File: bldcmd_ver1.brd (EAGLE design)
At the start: 43 x 49 mm, 84 parts, among them CN1 DF61-2P-2.2V(23), CN2 DF65-3P-1.7V(21), CN3 DF57H-5P-1.2V(21), CN5 SM04B-SRSS-TB, CN6 SM05B-SRSS-TB, CN7 SM04B-SRSS-TB, IC1 STSPIN32F0A, IC2 AS5047P-ATSM, IC4 LTC485S, Q1 PSMN2R4-30MLD, Q2 PSMN2R4-30MLD, Q3 PSMN2R4-30MLD, Q4 PSMN2R4-30MLD, Q5 PSMN2R4-30MLD, Q6 PSMN2R4-30MLD, SW1 SKRP

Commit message: AW進捗
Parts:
- moved R6 2.71 mm to (6.00, 16.2)
- moved R3 0.70 mm to (7.00, 33.0)
- moved R27 0.20 mm to (20.1, 1.50)
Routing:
- net GND: track 283.1 -> 298.8 mm
- net MOT_U: track 43.8 -> 47.3 mm, vias 11 -> 14
- net N$16: track 1.35 -> 4.26 mm
- net LS_W: track 15.1 -> 12.3 mm
- net MOT_W: track 39.1 -> 38.3 mm
- net OC_COMP: track 4.51 -> 3.66 mm
- net N$13: track 3.35 -> 2.65 mm
- net LS_U: track 34.1 -> 33.4 mm

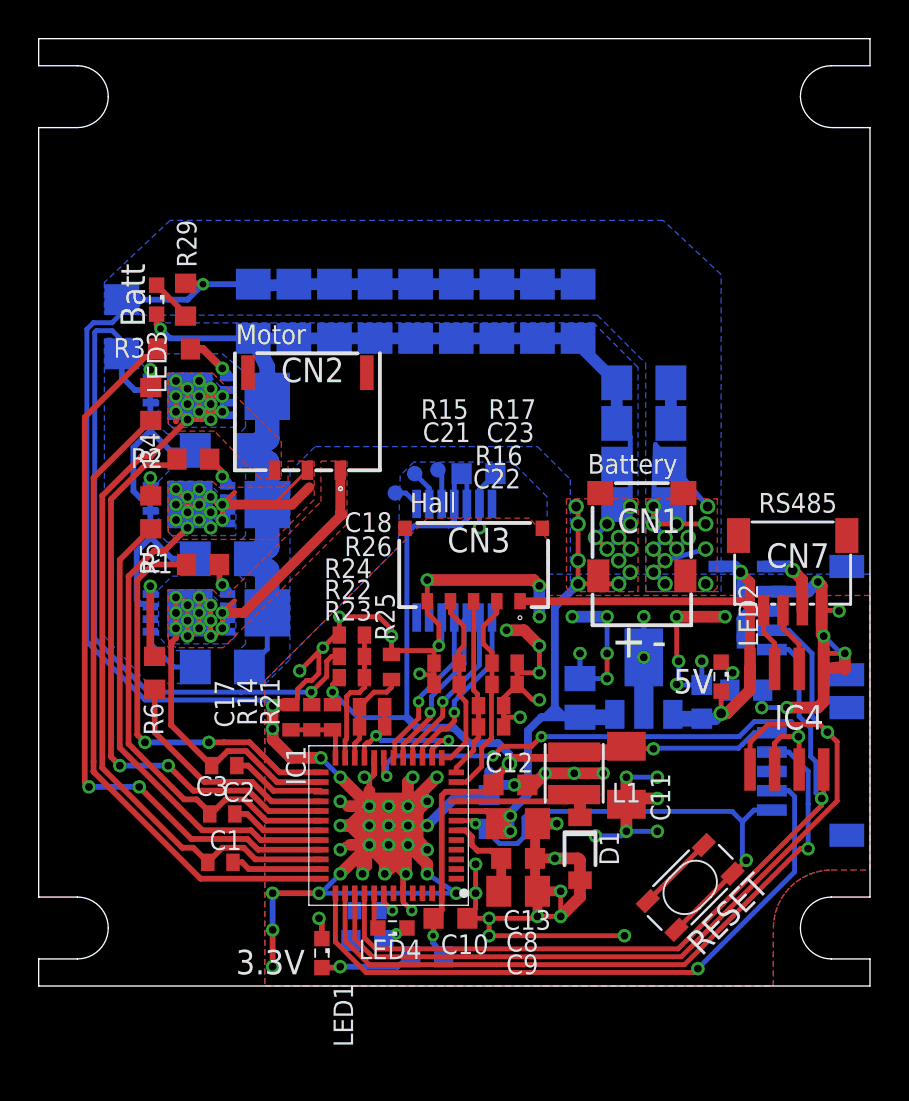
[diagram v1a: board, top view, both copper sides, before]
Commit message: 基板サイズを変更した
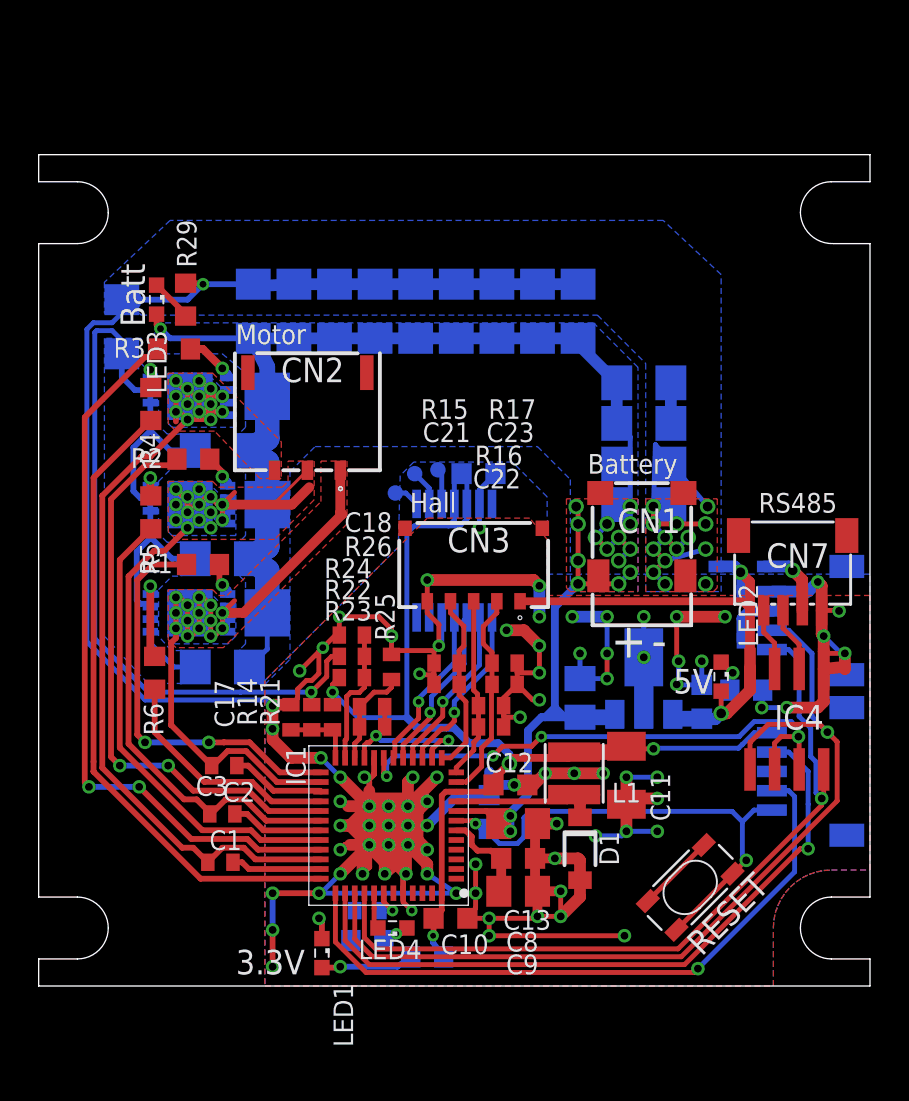
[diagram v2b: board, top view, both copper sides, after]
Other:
- board size 43 x 49 mm -> 43 x 43 mm
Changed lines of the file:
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@@
 <setting verticaltext="up"/>
 </settings>
-<grid distance="0.1" unitdist="mm" unit="mm" style="lines" multiple="1" display="yes" altdistance="0.05" altunitdist="mm" altunit="mm"/>
+<grid distance="1" unitdist="mm" unit="mm" style="lines" multiple="1" display="yes" altdistance="0.05" altunitdist="mm" altunit="mm"/>
 <layers>
-<layer number="1" name="Top" color="4" fill="1" visible="yes" active="yes"/>
+<layer number="1" name="Top" color="4" fill="1" visible="no" active="yes"/>
 <layer number="2" name="Route2" color="1" fill="3" visible="no" active="no"/>
 <layer number="3" name="Route3" color="4" fill="3" visible="no" active="no"/>
@@
 <layer number="19" name="Unrouted" color="6" fill="1" visible="yes" active="yes"/>
 <layer number="20" name="Dimension" color="24" fill="1" visible="yes" active="yes"/>
-<layer number="21" name="tPlace" color="31" fill="1" visible="yes" active="yes"/>
+<layer number="21" name="tPlace" color="31" fill="1" visible="no" active="yes"/>
 <layer number="22" name="bPlace" color="25" fill="10" visible="yes" active="yes"/>
-<layer number="23" name="tOrigins" color="15" fill="1" visible="yes" active="yes"/>
+<layer number="23" name="tOrigins" color="15" fill="1" visible="no" active="yes"/>
 <layer number="24" name="bOrigins" color="15" fill="1" visible="yes" active="yes"/>
 <layer number="25" name="tNames" color="11" fill="7" visible="no" active="yes"/>
-<layer number="26" name="bNames" color="13" fill="7" visible="no" active="yes"/>
+<layer number="26" name="bNames" color="13" fill="7" visible="yes" active="yes"/>
 <layer number="27" name="tValues" color="7" fill="1" visible="no" active="yes"/>
 <layer number="28" name="bValues" color="7" fill="1" visible="no" active="yes"/>
-<layer number="29" name="tStop" color="7" fill="3" visible="yes" active="yes"/>
+<layer number="29" name="tStop" color="7" fill="3" visible="no" active="yes"/>
 <layer number="30" name="bStop" color="7" fill="6" visible="yes" active="yes"/>
 <layer number="31" name="tCream" color="7" fill="4" visible="no" active="yes"/>
@@
 <layer number="37" name="tTest" color="7" fill="1" visible="no" active="yes"/>
 <layer number="38" name="bTest" color="7" fill="1" visible="no" active="yes"/>
-<layer number="39" name="tKeepout" color="4" fill="11" visible="yes" active="yes"/>
+<layer number="39" name="tKeepout" color="4" fill="11" visible="no" active="yes"/>
 <layer number="40" name="bKeepout" color="1" fill="11" visible="yes" active="yes"/>
 <layer number="41" name="tRestrict" color="4" fill="10" visible="no" active="yes"/>
@@
 <layer number="47" name="Measures" color="7" fill="1" visible="yes" active="yes"/>
 <layer number="48" name="Document" color="7" fill="1" visible="yes" active="yes"/>
-<layer number="49" name="Reference" color="18" fill="1" visible="yes" active="yes"/>
+<layer number="49" name="Reference" color="18" fill="1" visible="no" active="yes"/>
 <layer number="50" name="dxf" color="7" fill="1" visible="yes" active="yes"/>
-<layer number="51" name="tDocu" color="14" fill="1" visible="yes" active="yes"/>
+<layer number="51" name="tDocu" color="14" fill="1" visible="no" active="yes"/>
 <layer number="52" name="bDocu" color="11" fill="1" visible="yes" active="yes"/>
 <layer number="53" name="tGND_GNDA" color="7" fill="1" visible="yes" active="yes"/>
@@
 </layers>
 <board>
-<fusionsync huburn="a.cGVyc29uYWw6dWUyOTdmOTdk" projecturn="a.cGVyc29uYWw6dWUyOTdmOTdkIzIwMTYwMTIwMjMzNzY0MzE" f3durn="urn:adsk.wipprod:dm.lineage:Rlxp0FusTXWNQhIXcPZ1tQ" pcbguid="3740698e-3e28-4753-a590-d83306e07c12" lastpulledtime="" lastsyncedchangeguid="09eb6062-57fd-4b9e-7a9e-39c488cf4b4b"/>
+<fusionsync huburn="a.cGVyc29uYWw6dWUyOTdmOTdk" projecturn="a.cGVyc29uYWw6dWUyOTdmOTdkIzIwMTYwMTIwMjMzNzY0MzE" f3durn="urn:adsk.wipprod:dm.lineage:Rlxp0FusTXWNQhIXcPZ1tQ" pcbguid="3740698e-3e28-4753-a590-d83306e07c12" lastpulledtime="" lastsyncedchangeguid="25f6fb32-d5f4-c03e-7a0e-6774be7ba0ba"/>
 <plain>
 <wire x1="0" y1="0" x2="43" y2="0" width="0" layer="20"/>
@@
 BLDC_MotorDriver
 v1.1</text>
-<dimension x1="0" y1="0" x2="43" y2="0" x3="21.5" y3="-19.4" textsize="1.778" layer="48"/>
-<dimension x1="0" y1="0" x2="0" y2="49" x3="-10.8" y3="24.5" textsize="1.778" layer="48"/>
-<dimension x1="0" y1="49" x2="43" y2="49" x3="21.5" y3="60.8" textsize="1.778" layer="48"/>
-<dimension x1="43" y1="49" x2="43" y2="0" x3="63.8" y3="24.5" textsize="1.778" layer="48"/>
+<dimension x1="0" y1="-1" x2="43" y2="-1" x3="21.5" y3="-8.4" textsize="1.778" layer="48"/>
+<dimension x1="-1" y1="0" x2="-1" y2="43" x3="-6.8" y3="21.5" textsize="1.778" layer="48"/>
+<dimension x1="0" y1="44" x2="43" y2="44" x3="21.5" y3="48.8" textsize="1.778" layer="48"/>
+<dimension x1="44" y1="43" x2="44" y2="0" x3="50.800003125" y3="21.5" textsize="1.778" layer="48"/>
 <wire x1="43" y1="0" x2="43" y2="1.4" width="0" layer="20"/>
 <wire x1="43" y1="1.4" x2="41" y2="1.4" width="0" layer="20"/>
@@
 <wire x1="39.4" y1="3" x2="41" y2="4.6" width="0" layer="20" curve="-90"/>
 <wire x1="41" y1="4.6" x2="43" y2="4.6" width="0" layer="20"/>
-<wire x1="43" y1="4.6" x2="43" y2="44.4" width="0" layer="20"/>
-<wire x1="43" y1="44.4" x2="41.1" y2="44.4" width="0" layer="20"/>
-<wire x1="41.1" y1="44.4" x2="39.4" y2="46" width="0" layer="20" curve="-90"/>
-<wire x1="39.4" y1="46" x2="41" y2="47.6" width="0" layer="20" curve="-90"/>
-<wire x1="41" y1="47.6" x2="43" y2="47.6" width="0" layer="20"/>
-<wire x1="43" y1="47.6" x2="43" y2="49" width="0" layer="20"/>
-<wire x1="43" y1="49" x2="0" y2="49" width="0" layer="20"/>
-<wire x1="0" y1="49" x2="0" y2="47.6" width="0" layer="20"/>
-<wire x1="0" y1="47.6" x2="2" y2="47.6" width="0" layer="20"/>
-<wire x1="2" y1="47.6" x2="3.6" y2="46" width="0" layer="20" curve="-90"/>
-<wire x1="3.6" y1="46" x2="2" y2="44.4" width="0" layer="20" curve="-90"/>
-<wire x1="2" y1="44.4" x2="0" y2="44.4" width="0" layer="20"/>
-<wire x1="0" y1="44.4" x2="0" y2="4.6" width="0" layer="20"/>
+<wire x1="43" y1="4.6" x2="43" y2="38.4" width="0" layer="20"/>
+<wire x1="43" y1="38.4" x2="41.1" y2="38.4" width="0" layer="20"/>
+<wire x1="41.1" y1="38.4" x2="39.4" y2="40" width="0" layer="20" curve="-90"/>
+<wire x1="39.4" y1="40" x2="41" y2="41.6" width="0" layer="20" curve="-90"/>
+<wire x1="41" y1="41.6" x2="43" y2="41.6" width="0" layer="20"/>
+<wire x1="43" y1="41.6" x2="43" y2="43" width="0" layer="20"/>
+<wire x1="43" y1="43" x2="0" y2="43" width="0" layer="20"/>
+<wire x1="0" y1="43" x2="0" y2="41.6" width="0" layer="20"/>
+<wire x1="0" y1="41.6" x2="2" y2="41.6" width="0" layer="20"/>
+<wire x1="2" y1="41.6" x2="3.6" y2="40" width="0" layer="20" curve="-90"/>
+<wire x1="3.6" y1="40" x2="2" y2="38.4" width="0" layer="20" curve="-90"/>
+<wire x1="2" y1="38.4" x2="0" y2="38.4" width="0" layer="20"/>
+<wire x1="0" y1="38.4" x2="0" y2="4.6" width="0" layer="20"/>
 <wire x1="0" y1="4.6" x2="2" y2="4.6" width="0" layer="20"/>
 <wire x1="2" y1="4.6" x2="3.6" y2="3" width="0" layer="20" curve="-90"/>
@@
 <wire x1="2" y1="1.4" x2="0" y2="1.4" width="0" layer="20"/>
 <wire x1="0" y1="1.4" x2="0" y2="0" width="0" layer="20"/>
-<dimension x1="41" y1="46" x2="2" y2="46" x3="21.5" y3="50" textsize="1.778" layer="48"/>
-<circle x="41" y="46" radius="1.6" width="0.1016" layer="49"/>
-<wire x1="39" y1="46" x2="43" y2="46" width="0.1016" layer="49"/>
-<wire x1="41" y1="48" x2="41" y2="44" width="0.1016" layer="49"/>
-<wire x1="2" y1="48" x2="2" y2="44" width="0.1016" layer="49"/>
-<circle x="2" y="46" radius="1.6" width="0.1016" layer="49"/>
-<wire x1="4" y1="46" x2="0" y2="46" width="0.1016" layer="49"/>
-<wire x1="43" y1="48" x2="43" y2="44" width="0.1016" layer="49"/>
-<wire x1="0" y1="48" x2="0" y2="44" width="0.1016" layer="49"/>
+<dimension x1="41" y1="40" x2="2" y2="40" x3="21.5" y3="45" textsize="1.778" layer="48"/>
+<circle x="41" y="40" radius="1.6" width="0.1016" layer="49"/>
+<wire x1="39" y1="40" x2="43" y2="40" width="0.1016" layer="49"/>
+<wire x1="41" y1="42" x2="41" y2="38" width="0.1016" layer="49"/>
+<circle x="2" y="40" radius="1.6" width="0.1016" layer="49"/>
+<wire x1="4" y1="40" x2="0" y2="40" width="0.1016" layer="49"/>
 <wire x1="39" y1="3" x2="43" y2="3" width="0.1016" layer="49"/>
 <wire x1="41" y1="5" x2="41" y2="1" width="0.1016" layer="49"/>
@@
 <circle x="2" y="3" radius="1.6" width="0.1016" layer="49"/>
 <circle x="41" y="3" radius="1.6" width="0.1016" layer="49"/>
-<dimension x1="41" y1="46" x2="41" y2="3" x3="47" y3="24.5" textsize="1.778" layer="48"/>
-<dimension x1="2" y1="46" x2="2" y2="3" x3="-2" y3="24.5" textsize="1.778" layer="48"/>
+<dimension x1="41" y1="40" x2="41" y2="3" x3="47" y3="21.5" textsize="1.778" layer="48"/>
+<dimension x1="2" y1="40" x2="2" y2="3" x3="-2" y3="21.5" textsize="1.778" layer="48"/>
 <dimension x1="2" y1="3" x2="41" y2="3" x3="21.5" y3="-3" textsize="1.778" layer="48"/>
 <circle x="41" y="3" radius="3" width="0.1016" layer="49"/>
@@
 <wire x1="21.5" y1="22" x2="43.1" y2="43.6" width="0.254" layer="49"/>
 <wire x1="43.1" y1="43.6" x2="-0.1" y2="43.6" width="0.254" layer="49"/>
-<circle x="2" y="46" radius="3" width="0.1016" layer="49"/>
-<circle x="41" y="46" radius="3" width="0.1016" layer="49"/>
+<circle x="2" y="40" radius="3" width="0.1016" layer="49"/>
+<circle x="41" y="40" radius="3" width="0.1016" layer="49"/>
 <wire x1="2" y1="44" x2="2" y2="36.9" width="0.127" layer="49"/>
 </plain>

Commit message: AW進捗
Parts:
- moved R13 1.40 mm to (5.70, 34.1), turned to 315 degrees
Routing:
- net GND: track 298.8 -> 340.3 mm, vias 102 -> 118
- net OP_P: track 60.1 -> 61.0 mm

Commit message: AW進捗，これで発注
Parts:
- moved LED3 2.53 mm to (8.60, 35.1)
- moved R2 2.20 mm to (5.80, 27.2)
- moved R1 1.80 mm to (6.70, 21.8)
- moved R5 1.20 mm to (4.60, 24.5)
- moved R4 1.14 mm to (4.70, 30.4), turned to 45 degrees
- moved R3 0.61 mm to (7.60, 32.9)
- moved R29 0.51 mm to (7.10, 35.4)
- moved R27 0.22 mm to (20.0, 1.70)
- moved R18 0.05 mm to (16.9, 3.90)
- moved R19 0.05 mm to (16.9, 2.35)
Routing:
- net GND: track 340.3 -> 345.3 mm, vias 118 -> 123
- net N$11: track 1.76 -> 3.81 mm
- net N$9: track 1.70 -> 3.56 mm
- net +12V: track 88.6 -> 90.4 mm, vias 17 -> 22
- net HS_W: track 21.2 -> 19.4 mm
- net HS_V: track 29.6 -> 27.9 mm
- net MOT_U: track 47.3 -> 48.0 mm
- net N$15: track 1.35 -> 1.97 mm
- net MOT_V: track 52.6 -> 53.2 mm
- net N$13: track 2.65 -> 2.11 mm
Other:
- board text added: "SWD"

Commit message: 電解コンデンサのパターンを追加
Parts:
- added C35, C36, C37, C38: (no value), rcl:153CLV-0605
- C21, C22, C23: value 10p -> 470p
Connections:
- net +12V: now also C35.+, C36.+, C37.+, C38.+
- net GND: now also C35.-, C36.-, C37.-, C38.-
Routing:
- net GND: track 345.3 -> 346.1 mm

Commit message: AW修正
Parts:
- moved C6 0.70 mm to (8.80, 16.5)
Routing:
- net OP_P: track 61.0 -> 60.3 mm
- net +12V: track 90.4 -> 91.0 mm
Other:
- board text added: "Scramble BLDC_MotorDriver for Maxon EC-Flat v1.2"
- board text removed: "Scramble BLDC_MotorDriver v1.1"
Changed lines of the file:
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@@
 <layer number="47" name="Measures" color="7" fill="1" visible="yes" active="yes"/>
 <layer number="48" name="Document" color="7" fill="1" visible="yes" active="yes"/>
-<layer number="49" name="Reference" color="18" fill="1" visible="no" active="yes"/>
+<layer number="49" name="Reference" color="18" fill="1" visible="yes" active="yes"/>
 <layer number="50" name="dxf" color="7" fill="1" visible="yes" active="yes"/>
 <layer number="51" name="tDocu" color="14" fill="1" visible="yes" active="yes"/>
@@
 <wire x1="21.5" y1="43.3" x2="21.5" y2="42.6" width="0.2" layer="22"/>
 <wire x1="5.8" y1="22" x2="0.2" y2="22" width="0.2" layer="22"/>
-<text x="18.7" y="30.2" size="1.016" layer="21" ratio="12">Scramble
+<text x="18.6" y="31.3" size="1.27" layer="21" ratio="12">Scramble
 BLDC_MotorDriver
-v1.1</text>
+for Maxon EC-Flat
+v1.2</text>
 <dimension x1="0" y1="-1" x2="43" y2="-1" x3="21.5" y3="-8.4" textsize="1.778" layer="48"/>
 <dimension x1="-1" y1="0" x2="-1" y2="43" x3="-6.8" y3="21.5" textsize="1.778" layer="48"/>
@@
 <wire x1="19.3" y1="22" x2="19.6" y2="22" width="0.2" layer="22"/>
 <wire x1="23.4" y1="22" x2="23.7" y2="22" width="0.2" layer="22"/>
+<polygon width="0.0762" layer="30">
+<vertex x="5.4" y="23.7"/>
+<vertex x="5.4" y="25.4"/>
+<vertex x="6.2" y="25.4"/>
+<vertex x="6.2" y="23.7"/>
+</polygon>
+<polygon width="0.0762" layer="30">
+<vertex x="5.4" y="19.8"/>
+<vertex x="6.2" y="19.8"/>
+<vertex x="6.2" y="18.1"/>
+<vertex x="5.4" y="18.1"/>
+</polygon>
+<polygon width="0.0762" layer="30">
+<vertex x="5.4" y="29.3"/>
+<vertex x="5.4" y="31"/>
+<vertex x="6.2" y="31"/>
+<vertex x="6.2" y="29.3"/>
+</polygon>
+<polygon width="0.0762" layer="30">
+<vertex x="9.4" y="29.3"/>
+<vertex x="10.2" y="29.3"/>
+<vertex x="10.2" y="31"/>
+<vertex x="9.4" y="31"/>
+</polygon>
+<polygon width="0.0762" layer="30">
+<vertex x="9.4" y="25.4"/>
+<vertex x="10.2" y="25.4"/>
+<vertex x="10.2" y="23.7"/>
+<vertex x="9.4" y="23.7"/>
+</polygon>
+<polygon width="0.0762" layer="30">
+<vertex x="9.4" y="19.8"/>
+<vertex x="10.2" y="19.8"/>
+<vertex x="10.2" y="18.1"/>
+<vertex x="9.4" y="18.1"/>
+</polygon>
 </plain>
 <attributes>
@@
 <attribute name="VALUE" x="10.77" y="25.16" size="1.27" layer="28" rot="MR0"/>
 </element>
-<element name="C6" library="rcl" library_urn="urn:adsk.eagle:library:334" package="C1206" package3d_urn="urn:adsk.eagle:package:23618/2" value="10u" x="9.5" y="16.5" smashed="yes" rot="MR0">
-<attribute name="NAME" x="12.1" y="15.5" size="1.016" layer="26" rot="MR90"/>
-<attribute name="VALUE" x="10.77" y="13.96" size="1.27" layer="28" rot="MR0"/>
+<element name="C6" library="rcl" library_urn="urn:adsk.eagle:library:334" package="C1206" package3d_urn="urn:adsk.eagle:package:23618/2" value="10u" x="8.8" y="16.5" smashed="yes" rot="MR0">
+<attribute name="NAME" x="11.4" y="15.5" size="1.016" layer="26" rot="MR90"/>
+<attribute name="VALUE" x="10.07" y="13.96" size="1.27" layer="28" rot="MR0"/>
 </element>
 <element name="R13" library="rcl" library_urn="urn:adsk.eagle:library:334" package="R3216" package3d_urn="urn:adsk.eagle:package:23557/2" value="0.01" x="5.7" y="34.1" smashed="yes" rot="MR315">
@@
 <vertex x="12.8" y="27.15"/>
 <vertex x="15" y="27.15"/>
-<vertex x="15" y="25.35"/>
-<vertex x="11.95" y="22.3"/>
+<vertex x="15" y="25.15"/>
+<vertex x="12.15" y="22.3"/>
 <vertex x="8.05" y="22.3"/>
 <vertex x="6.7" y="23.5"/>
@@
 <vertex x="6.7" y="20.5"/>
 <vertex x="8.1" y="21.9"/>
-<vertex x="12" y="21.9"/>
-<vertex x="15.35" y="25.25"/>
+<vertex x="12.2" y="21.9"/>
+<vertex x="15.35" y="25.05"/>
 <vertex x="15.35" y="27.15"/>
 <vertex x="17.6" y="27.15"/>
-<vertex x="17.6" y="23.8"/>
-<vertex x="11.3" y="17.5"/>
+<vertex x="17.6" y="23.6"/>
+<vertex x="11.5" y="17.5"/>
 <vertex x="7.1" y="17.5"/>
 <vertex x="6.7" y="17.9"/>
@@
 <contactref element="R22" pad="2"/>
 <via x="14.1" y="15.2" extent="1-16" drill="0.35"/>
-<wire x1="8.1" y1="16.5" x2="7" y2="16.5" width="0.254" layer="16"/>
+<wire x1="7.4" y1="16.5" x2="7" y2="16.5" width="0.254" layer="16"/>
 <wire x1="7" y1="16.5" x2="5.8" y2="17.7" width="0.254" layer="16"/>
 <wire x1="5.8" y1="17.7" x2="5.8" y2="18.3" width="0.254" layer="16"/>
@@
 <vertex x="10.4" y="21.2"/>
 <vertex x="10.7" y="20.9"/>
-<vertex x="10.7" y="17.7"/>
-<vertex x="10.4" y="17.4"/>
-<vertex x="10.4" y="15.6"/>
-<vertex x="11.5" y="15.6"/>
-<vertex x="14.4" y="18.5"/>
+<vertex x="10.7" y="18"/>
+<vertex x="10.1" y="17.4"/>
+<vertex x="10.1" y="15.6"/>
+<vertex x="11" y="15.6"/>
+<vertex x="14.4" y="19"/>
 <vertex x="14.4" y="22.5"/>
 <vertex x="19.6" y="27.7"/>
@@
 <wire x1="11.825" y1="32.025" x2="11.1" y2="33.5" width="0.8128" layer="16"/>
 <wire x1="11.825" y1="19.3" x2="11.825" y2="17.425" width="0.254" layer="16"/>
-<wire x1="11.825" y1="17.425" x2="10.9" y2="16.5" width="0.254" layer="16"/>
+<wire x1="11.825" y1="17.425" x2="10.2" y2="16.5" width="0.254" layer="16"/>
 <contactref element="C20" pad="1"/>
 <contactref element="LED3" pad="A"/>
